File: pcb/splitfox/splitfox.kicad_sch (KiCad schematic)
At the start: 137 parts, among them CN1 S7B-ZR-SM4A-TF(LF)(SN)_C51187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, CN2 S7B-ZR-SM4A-TF(LF)(SN)_C51187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, SW1 TS24CA, SW2 SS-12D07-L5-B, SW3 GT-TC152A-H085-L1, SW4 GT-TC152A-H085-L1, SW5 GT-TC152A-H085-L1, SW6 GT-TC152A-H085-L1, SW7 GT-TC152A-H085-L1, SW8 GT-TC152A-H085-L1, U1 RP2040, U2 SN74LV1T34DBVR, U3 W25Q128JVS, U4 XC6206PxxxMR-Regulator_Linear, U5 USBLC6-2SC6, Y1 12MHz

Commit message: NG | Splitfox PCB Placement
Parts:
- C13: value 10uF -> 100uF; LCSC C15525 -> C1525
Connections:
- net GND: now also CN2.8, CN2.9
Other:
- moved on the sheet: C13
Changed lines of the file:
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@@
 	(wire
 		(pts
+			(xy 195.58 85.09) (xy 203.835 85.09)
+		)
+		(stroke
+			(width 0)
+			(type default)
+		)
+	)
+	(wire
+		(pts
 			(xy 341.63 88.9) (xy 344.17 88.9)
 		)
@@
 	(wire
 		(pts
-			(xy 197.485 85.09) (xy 203.835 85.09)
-		)
-		(stroke
-			(width 0)
-			(type default)
-		)
-	)
-	(wire
-		(pts
 			(xy 368.3 151.13) (xy 369.57 151.13)
 		)
@@
 	(wire
 		(pts
+			(xy 195.58 91.44) (xy 195.58 92.71)
+		)
+		(stroke
+			(width 0)
+			(type default)
+		)
+	)
+	(wire
+		(pts
 			(xy 242.57 129.54) (xy 242.57 130.81)
 		)
@@
 	(wire
 		(pts
-			(xy 197.485 91.44) (xy 197.485 92.71)
-		)
-		(stroke
-			(width 0)
-			(type default)
-		)
-	)
-	(wire
-		(pts
 			(xy 194.31 123.19) (xy 196.85 123.19)
 		)
@@
 	(wire
 		(pts
-			(xy 197.485 92.71) (xy 203.835 92.71)
-		)
-		(stroke
-			(width 0)
-			(type default)
-		)
-	)
-	(wire
-		(pts
 			(xy 284.48 90.17) (xy 285.75 90.17)
 		)
@@
 	(wire
 		(pts
+			(xy 195.58 86.36) (xy 195.58 85.09)
+		)
+		(stroke
+			(width 0)
+			(type default)
+		)
+	)
+	(wire
+		(pts
 			(xy 210.185 92.71) (xy 213.995 92.71)
 		)
@@
 	(wire
 		(pts
-			(xy 197.485 86.36) (xy 197.485 85.09)
+			(xy 195.58 92.71) (xy 203.835 92.71)
 		)
 		(stroke
@@
 	(symbol
 		(lib_id "Device:C_Small")
-		(at 197.485 88.9 0)
+		(at 195.58 88.9 0)
 		(unit 1)
 		(exclude_from_sim no)
@@
 		(dnp no)
 		(property "Reference" "C13"
-			(at 198.755 86.3599 0)
+			(at 196.85 86.3599 0)
 			(effects
 				(font
@@
 			)
 		)
-		(property "Value" "10uF"
-			(at 198.755 91.4399 0)
+		(property "Value" "100uF"
+			(at 196.85 91.4399 0)
 			(effects
 				(font
@@
 		)
 		(property "Footprint" "Capacitor_SMD:C_0402_1005Metric"
-			(at 197.485 88.9 0)
+			(at 195.58 88.9 0)
 			(effects
 				(font
@@
 		)
 		(property "Datasheet" "~"
-			(at 197.485 88.9 0)
+			(at 195.58 88.9 0)
 			(effects
 				(font
@@
 		)
 		(property "Description" ""
-			(at 197.485 88.9 0)
+			(at 195.58 88.9 0)
 			(effects
 				(font
@@
 			)
 		)
-		(property "LCSC" "C15525"
-			(at 197.485 88.9 0)
+		(property "LCSC" "C1525"
+			(at 195.58 88.9 0)
 			(effects
 				(font
@@
 	)
 	(symbol
+		(lib_name "GND_10")
+		(lib_id "power:GND")
+		(at 257.81 34.29 90)
+		(unit 1)
+		(exclude_from_sim no)
+		(in_bom yes)
+		(on_board yes)
+		(dnp no)
+		(fields_autoplaced yes)
+		(property "Reference" "#PWR0150"
+			(at 264.16 34.29 0)
+			(effects
+				(font
+					(size 1.27 1.27)
+				)
+				(hide yes)
+			)
+		)
+		(property "Value" "GND"
+			(at 261.62 34.2899 90)
+			(effects
+				(font
+					(size 1.27 1.27)
+				)
+				(justify right)
+			)
+		)
+		(property "Footprint" ""
+			(at 257.81 34.29 0)
+			(effects
+				(font
+					(size 1.27 1.27)
+				)
+				(hide yes)
+			)
+		)
+		(property "Datasheet" ""
+			(at 257.81 34.29 0)
+			(effects
+				(font
+					(size 1.27 1.27)
+				)
+				(hide yes)
+			)
+		)
+		(property "Description" "Power symbol creates a global label with name \"GND\" , ground"
+			(at 257.81 34.29 0)
+			(effects
+				(font
+					(size 1.27 1.27)
+				)
+				(hide yes)
+			)
+		)
+		(pin "1"
+		)
+		(instances
+			(project ""
+				(path "/ba62e47e-9e07-4e97-ab08-24b670d50f97"
+					(reference "#PWR0150")
+					(unit 1)
+				)
+			)
+		)
+	)
+	(symbol
 		(lib_name "GND_6")
 		(lib_id "power:GND")
@@
 					(unit 1)
 				)
+			)
+		)
+	)
+	(symbol
+		(lib_name "GND_10")
+		(lib_id "power:GND")
+		(at 232.41 34.29 270)
+		(unit 1)
+		(exclude_from_sim no)
+		(in_bom yes)
+		(on_board yes)
+		(dnp no)
+		(fields_autoplaced yes)
+		(property "Reference" "#PWR0151"
+			(at 226.06 34.29 0)
+			(effects
+				(font
+					(size 1.27 1.27)
+				)
+				(hide yes)
+			)
+		)
+		(property "Value" "GND"
+			(at 228.6 34.2899 90)
+			(effects
+				(font
+					(size 1.27 1.27)
+				)
+				(justify right)
+			)
+		)
+		(property "Footprint" ""
+			(at 232.41 34.29 0)
+			(effects
+				(font
+					(size 1.27 1.27)
+				)
+				(hide yes)
+			)
+		)
+		(property "Datasheet" ""
+			(at 232.41 34.29 0)
+			(effects
+				(font
+					(size 1.27 1.27)
+				)
+				(hide yes)
+			)
+		)
+		(property "Description" "Power symbol creates a global label with name \"GND\" , ground"
+			(at 232.41 34.29 0)
+			(effects
+				(font
+					(size 1.27 1.27)
+				)
+				(hide yes)
+			)
+		)
+		(pin "1"
+		)
+		(instances
+			(project "splitfox"
+				(path "/ba62e47e-9e07-4e97-ab08-24b670d50f97"
+					(reference "#PWR0151")
+					(unit 1)
+				)

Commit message: NG | SplitFox PCB, Redid body cad
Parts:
- C13: value 100uF -> 100nF
- C6, C7: value 30pF -> 15pF; LCSC C1570 -> C106997
- LOGO2: footprint PicoFoxpretty:picofox -> PicoFoxpretty:picofox_small
- Y1: LCSC C9002 -> C20625731
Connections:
- net GND: now also CN1.8, CN1.9, FPC1.31, FPC1.32, SW1.1, SW1.2, SW2.EH, SW3.3 (C), SW4.3 (C), SW5.3 (C), SW6.3 (C), SW7.3 (C), SW8.3 (C), USB1.5, USB1.6, USB1.7, USB1.8
- net GPIO10: now also CH12.1; no longer CH10.1
- net GPIO11: now also CH10.1; no longer CH8.1
- net GPIO12: now also CH8.1; no longer CH6.1
- net GPIO13: now also CH6.1; no longer CH4.1
- net GPIO16: now also CH7.1; no longer CH11.1
- net GPIO18: now also CH11.1; no longer CH7.1
- net GPIO23: now also SW3.2 (B)
- net GPIO24: now also SW5.2 (B)
- net GPIO25: now also SW7.2 (B)
- net GPIO6: now also SW4.2 (B)
- net GPIO7: now also SW6.2 (B)
- net GPIO8: now also SW8.2 (B)
- net GPIO9: now also CH4.1; no longer CH12.1
- net LED_DATA_END: now also LED21.2 (DOUT); no longer LED28.2 (DOUT)
- net at LED24.2 (DOUT): now also LED17.3 (DIN); no longer LED4.3 (DIN)
- net at LED24.3 (DIN): now also LED4.2 (DOUT); no longer LED17.2 (DOUT)
- net at LED11.3 (DIN): now also LED18.2 (DOUT); no longer LED4.2 (DOUT)
- net at LED26.2 (DOUT): now also LED19.3 (DIN); no longer LED6.3 (DIN)
- net at LED26.3 (DIN): now also LED6.2 (DOUT); no longer LED19.2 (DOUT)
- net at LED25.2 (DOUT): now also LED18.3 (DIN); no longer LED5.3 (DIN)
- net at LED25.3 (DIN): now also LED5.2 (DOUT); no longer LED18.2 (DOUT)
- net at LED13.2 (DOUT): now also LED6.3 (DIN); no longer LED20.3 (DIN)
- net at LED13.3 (DIN): now also LED20.2 (DOUT); no longer LED6.2 (DOUT)
- net at LED12.3 (DIN): now also LED10.2 (DOUT); no longer LED5.2 (DOUT)
- net at LED12.2 (DOUT): now also LED5.3 (DIN); no longer LED19.3 (DIN)
- net at LED11.2 (DOUT): now also LED4.3 (DIN); no longer LED18.3 (DIN)
- net at LED14.2 (DOUT): now also LED7.3 (DIN); no longer LED21.3 (DIN)
- net at LED14.3 (DIN): now also LED17.2 (DOUT); no longer LED7.2 (DOUT)
- net at LED27.2 (DOUT): now also LED20.3 (DIN); no longer LED7.3 (DIN)
- net at LED28.3 (DIN): now also LED19.2 (DOUT); no longer LED21.2 (DOUT)
- net at LED27.3 (DIN): now also LED7.2 (DOUT); no longer LED20.2 (DOUT)
- new net: LED21.3 (DIN), LED28.2 (DOUT)
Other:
- moved on the sheet: C29, C30, C31, C32, C36, C37, C38, C39, C42, C43, C44, C45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

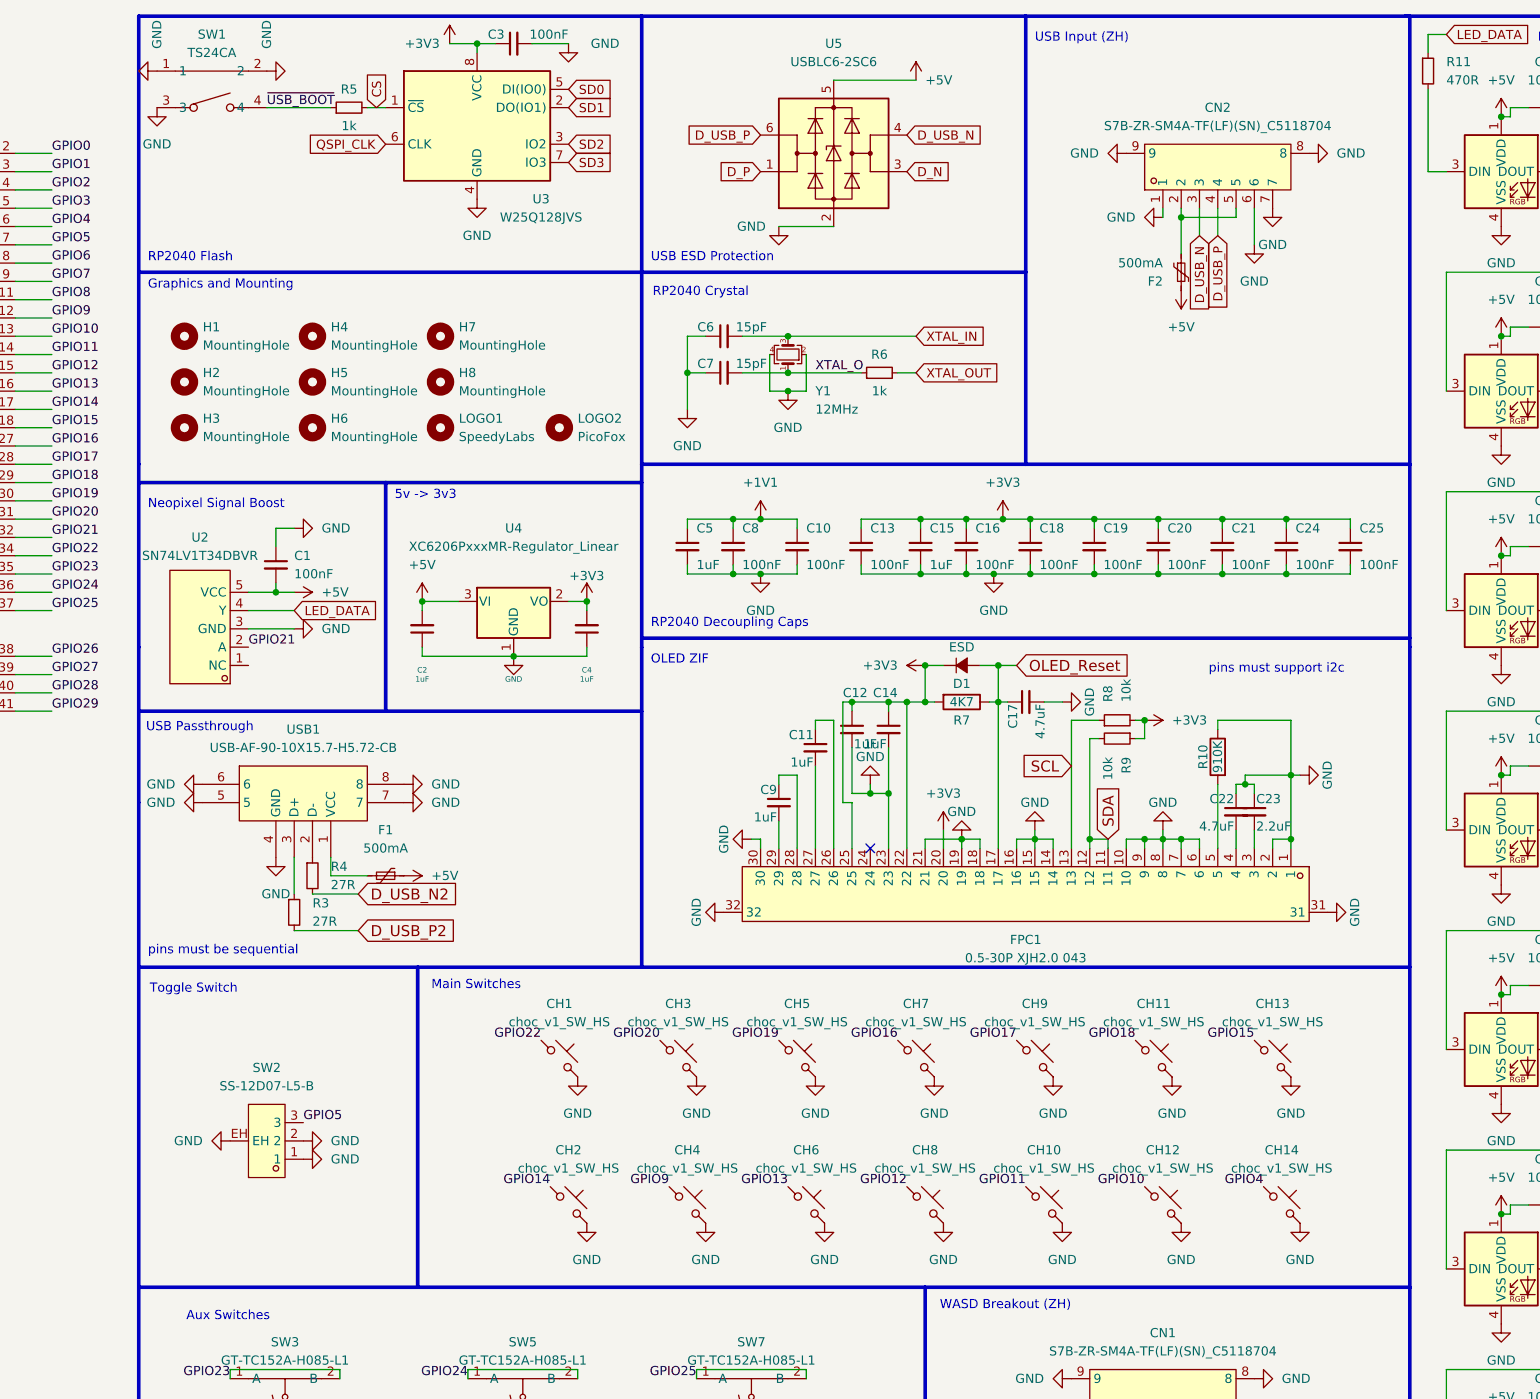
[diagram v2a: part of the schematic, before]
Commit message: NG | ESD/EMI caps, USB C flash port
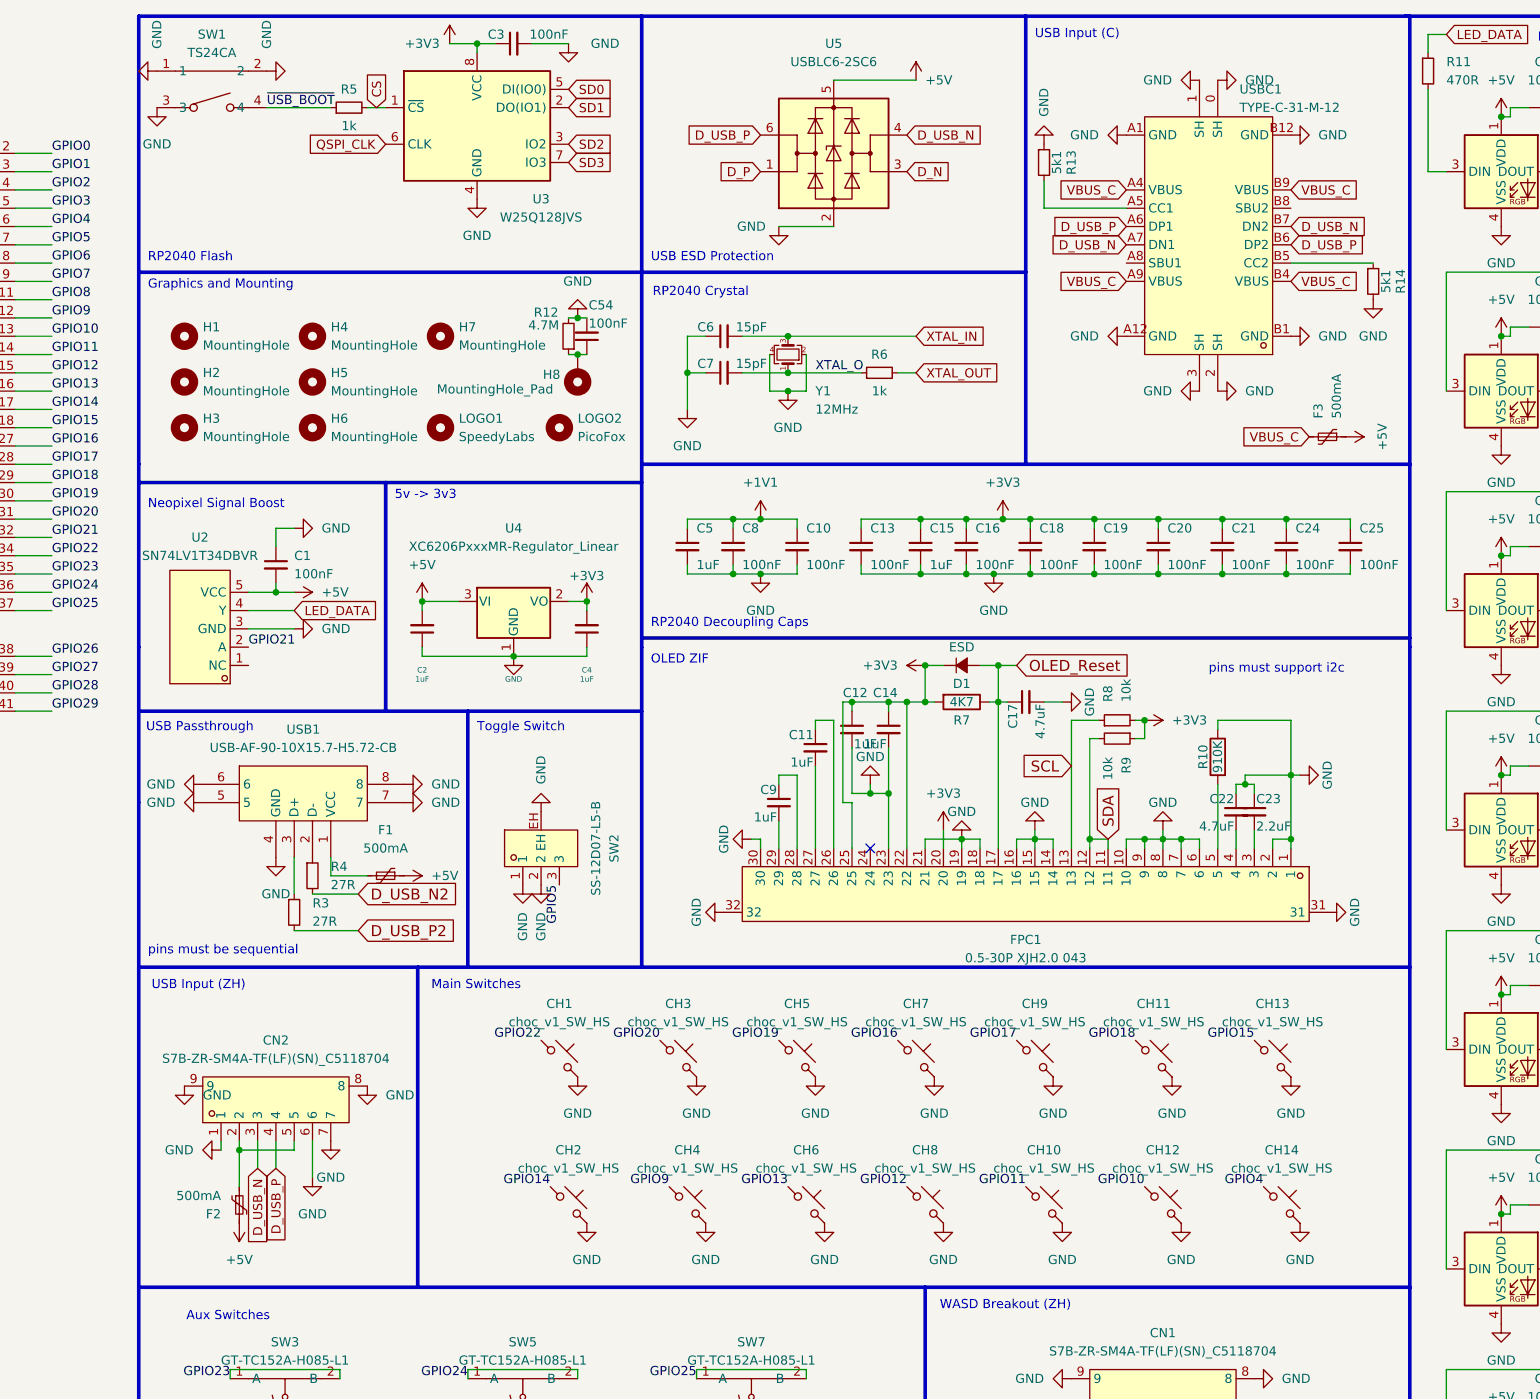
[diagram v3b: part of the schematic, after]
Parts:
- removed H8: MountingHole, MountingHole:MountingHole_3mm, symbol Mechanical:MountingHole
- added C54: 100nF, Capacitor_SMD:C_0402_1005Metric, symbol Device:C_Small
- added F3: 500mA, Fuse:Fuse_1206_3216Metric, symbol Device:Polyfuse_Small
- added H8: MountingHole_Pad, MountingHole:MountingHole_3mm_Pad, symbol Mechanical:MountingHole_Pad
- added R12: 4.7M, Resistor_SMD:R_0402_1005Metric, symbol Device:R_Small
- added R13, R14: 5k1, Resistor_SMD:R_0402_1005Metric, symbol Device:R_Small
- added USBC1: TYPE-C-31-M-12, easyeda:USB-C_SMD-TYPE-C-31-M-12, symbol easyeda:TYPE-C-31-M-12
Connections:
- net +5V: now also F3.1
- net D_USB_N: now also USBC1.A7 (DN1), USBC1.B7 (DN2)
- net D_USB_P: now also USBC1.A6 (DP1), USBC1.B6 (DP2)
- net GND: now also C54.2, R12.2, R13.1, R14.2, USBC1.0 (SH), USBC1.1 (SH), USBC1.2 (SH), USBC1.3 (SH), USBC1.A1 (GND), USBC1.A12 (GND), USBC1.B1 (GND), USBC1.B12 (GND)
- new net: C54.1, H8.1, R12.1
- new net: R14.1, USBC1.B5 (CC2)
- new net: R13.2, USBC1.A5 (CC1)
- new net VBUS_C: F3.2, USBC1.A4 (VBUS), USBC1.A9 (VBUS), USBC1.B4 (VBUS), USBC1.B9 (VBUS)
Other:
- note added: "USB Input (C)"
- moved on the sheet: CN2, F2, SW2

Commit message: NG | v1.1 SplitFox PCB - old crystal setup test
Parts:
- C6, C7: value 15pF -> 30pF; LCSC C106997 -> C1570
- Y1: LCSC C20625731 -> C9002
